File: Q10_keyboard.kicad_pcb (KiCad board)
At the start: 2 copper layers, 68 x 48 mm, 33 parts, among them J1 Conn_01x04, J2 Conn_01x04, J3 Conn_01x04, P1 USB_C_Plug_USB2.0, Q1 BSS138, SW1 SW_SPDT, U1 STM32F103C8Tx, U2 SRV05-4, U3 MIC5219-3.3YM5, U4 BBQ10KBD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

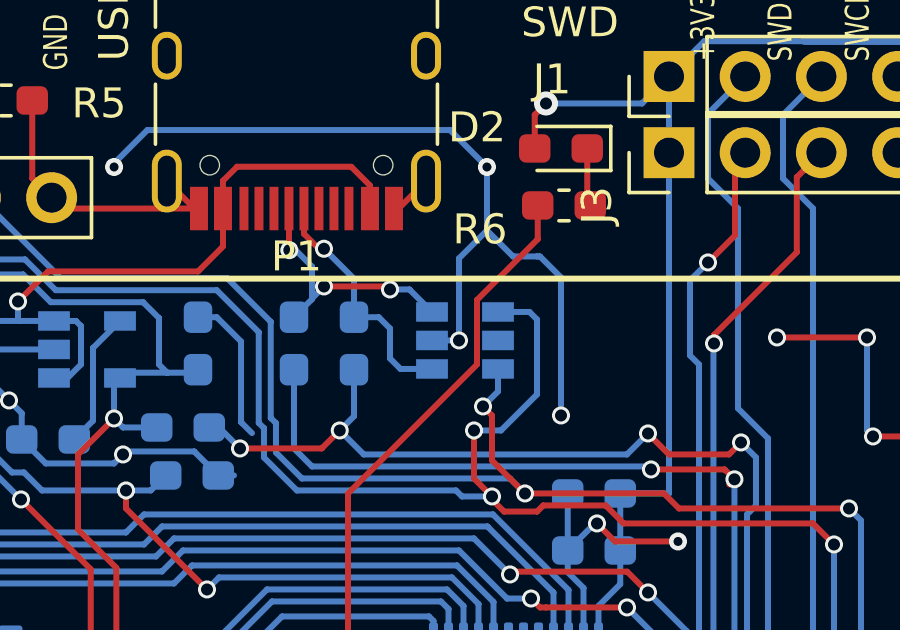
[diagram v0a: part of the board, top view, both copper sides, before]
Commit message: Add 5.1k pull-down on USB Type-C CC1 pin
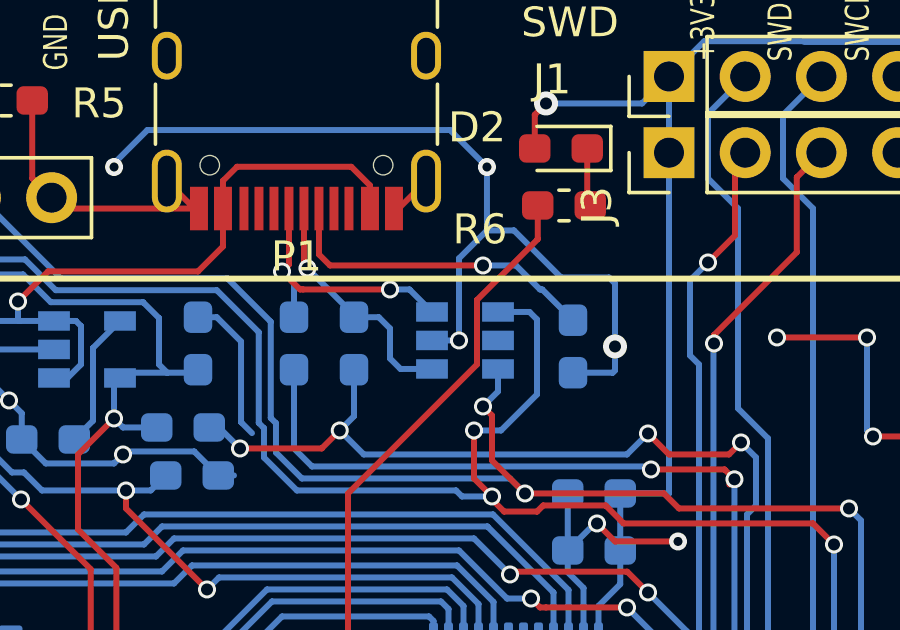
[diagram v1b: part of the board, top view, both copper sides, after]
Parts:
- added R10: 5.1K, Resistor_SMD:R_0603_1608Metric_Pad1.05x0.95mm_HandSolder, B.Cu at (58.3, 27.5)
- P1: value USB_C_Plug_USB2.0 -> USB_C_Plug_USB2.0-Connector; footprint Connector_USB:USB_C_Receptacle_HRO_TYPE-C-31-M-12 -> Q10_keyboard:USB_C_Receptacle_HRO_TYPE-C-31-M-12
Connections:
- P1 pad A5: Net-(P1-PadA5) -> /CC1
- P1 pad A8: (no net) -> Net-(P1-PadA8)
- SW1 pad : GND -> (no net)
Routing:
- net /CC1: track 0.00 -> 10.9 mm, vias 0 -> 1
- net GND: track 360.3 -> 361.9 mm
- net Net-(P1-PadA7): track 8.86 -> 9.87 mm, vias 3 -> 2
